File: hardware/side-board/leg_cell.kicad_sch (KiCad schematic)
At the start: 88 parts, among them IC201 STM32C092KCT6, IC202 TCAN332DR, IC203 TPS56A37RPAR, IC204 INA181A1IDBVR, J201 Servo Connector, J202 Servo Connector, J203 Servo Connector, J205 Conn_01x04, Y201 Crystal_GND24

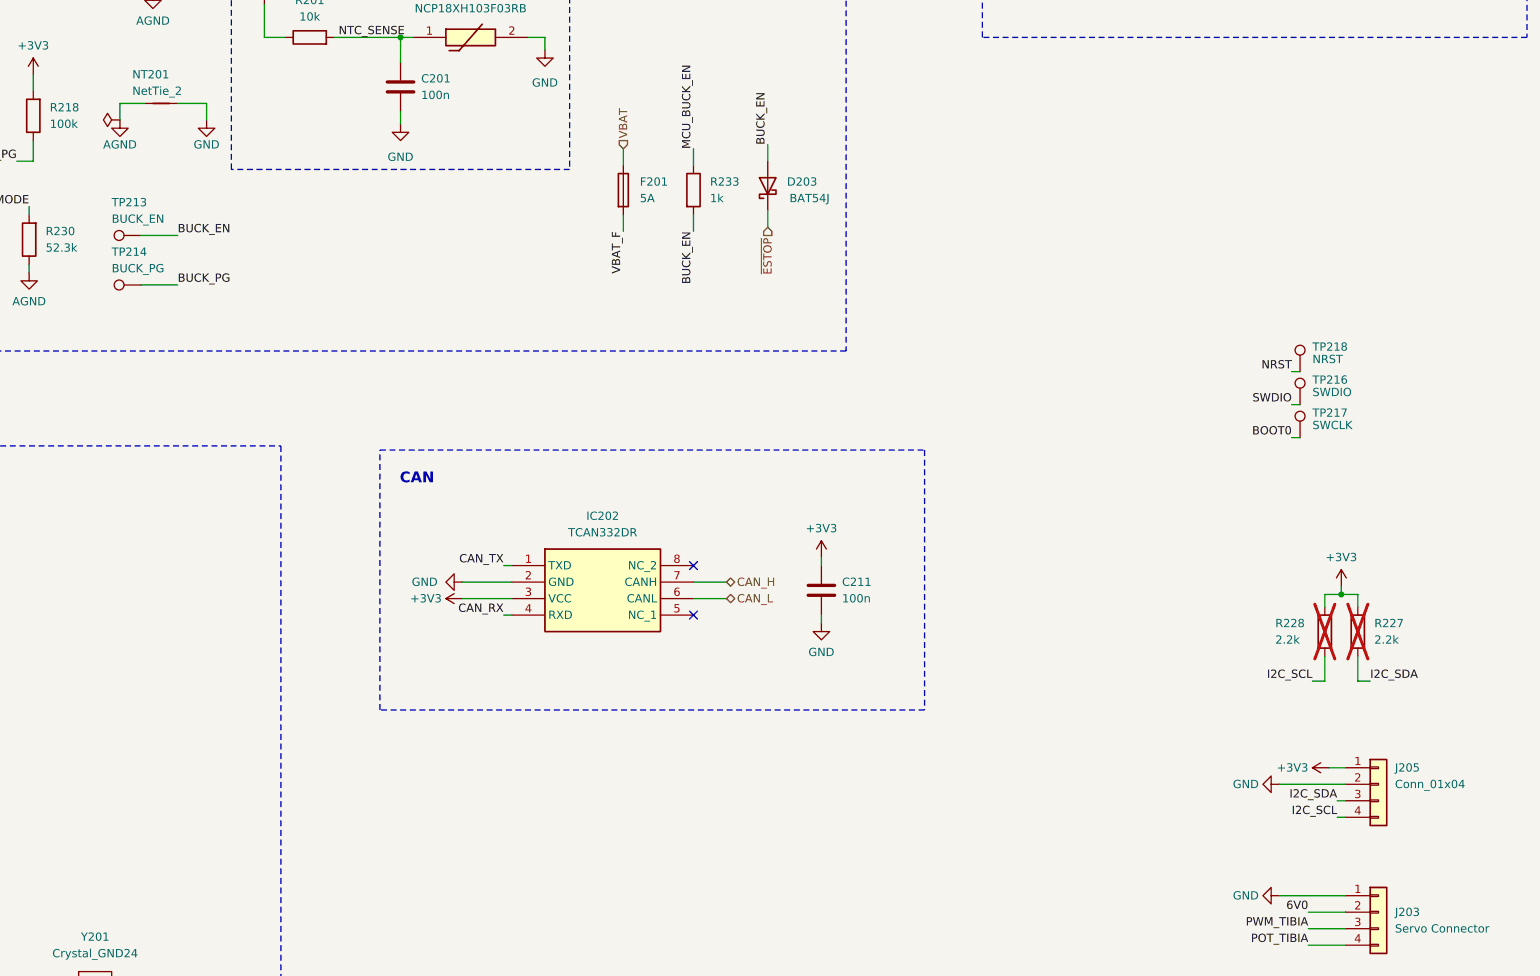
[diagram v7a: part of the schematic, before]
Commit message: Compacted sideboard further
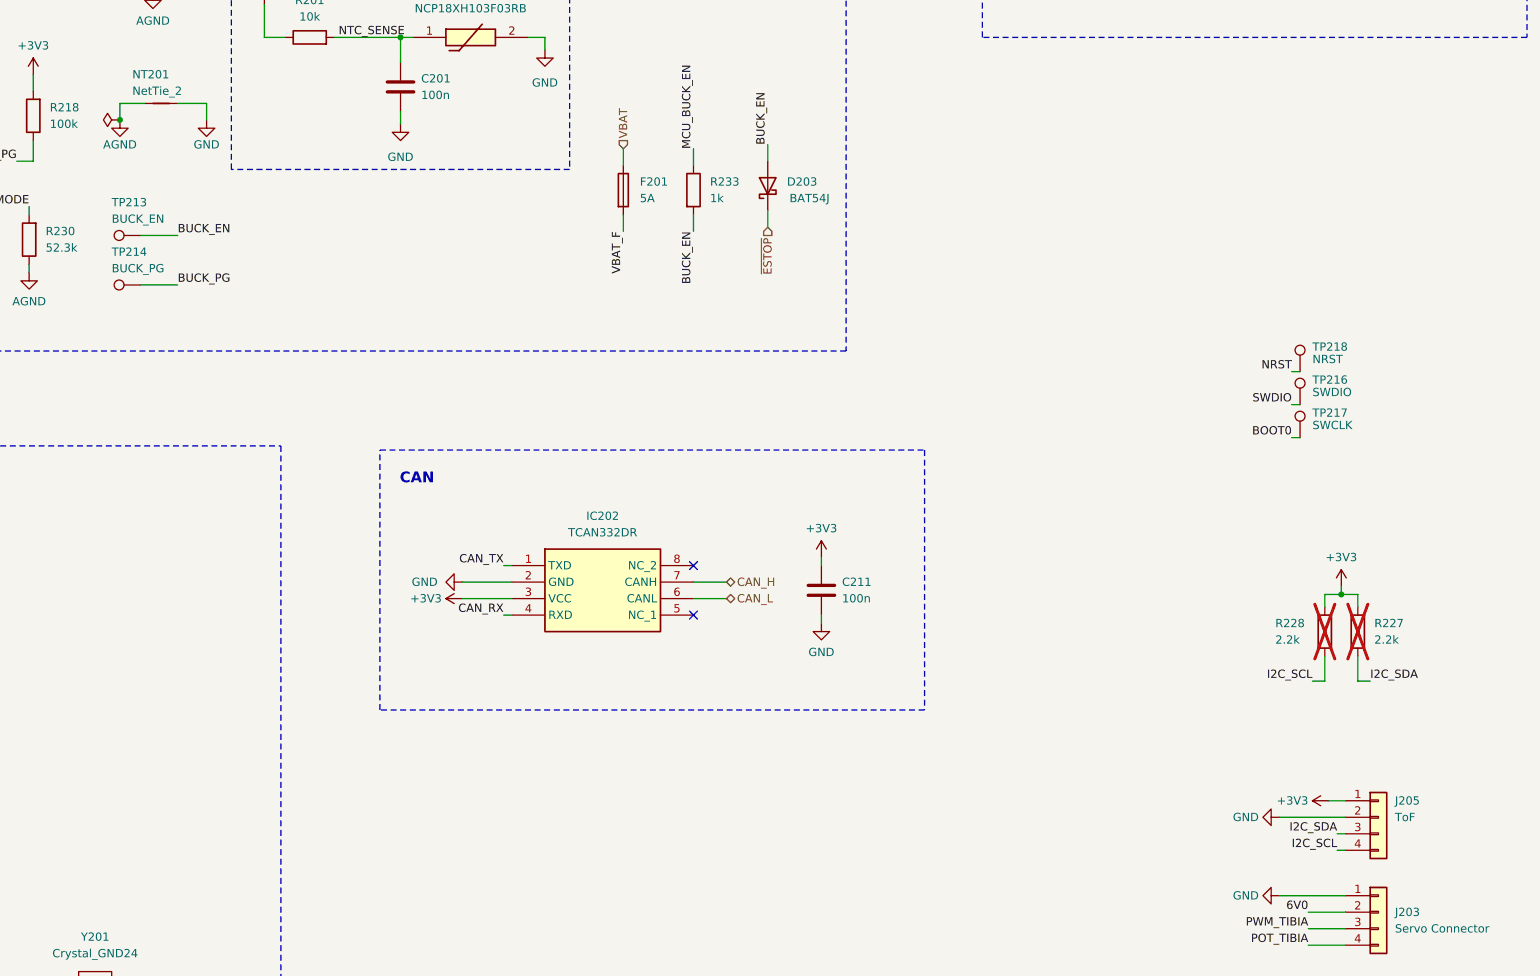
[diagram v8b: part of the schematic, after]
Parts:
- J201, J202, J203: footprint Connector_JST:JST_XH_B4B-XH-A_1x04_P2.50mm_Vertical -> vector:PinHeader_1x04_P2.54mm_Vertical_Tile
- J205: value Conn_01x04 -> ToF; footprint Connector_JST:JST_XH_B4B-XH-A_1x04_P2.50mm_Vertical -> vector:PinHeader_1x04_P2.54mm_Vertical_Tile
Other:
- moved on the sheet: J205
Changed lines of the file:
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@@
 	)
 	(junction
+		(at 184.15 86.36)
+		(diameter 0)
+		(color 0 0 0 0)
+	)
+	(junction
 		(at 260.35 43.18)
 		(diameter 0)
@@
 	)
 	(no_connect
-		(at 76.2 39.37)
+		(at 272.415 162.56)
 	)
 	(no_connect
@@
 	)
 	(no_connect
-		(at 272.415 162.56)
+		(at 272.415 154.94)
 	)
 	(no_connect
-		(at 272.415 154.94)
+		(at 76.2 39.37)
 	)
 	(wire
@@
 	(wire
 		(pts
-			(xy 362.585 188.595) (xy 372.745 188.595)
+			(xy 362.585 193.675) (xy 372.745 193.675)
 		)
 		(stroke
@@
 	(wire
 		(pts
-			(xy 371.475 193.675) (xy 372.745 193.675)
+			(xy 371.475 198.755) (xy 372.745 198.755)
 		)
 		(stroke
@@
 	(wire
 		(pts
-			(xy 370.205 186.055) (xy 372.745 186.055)
+			(xy 370.205 191.135) (xy 372.745 191.135)
 		)
 		(stroke
@@
 	(wire
 		(pts
-			(xy 371.475 191.135) (xy 372.745 191.135)
+			(xy 371.475 196.215) (xy 372.745 196.215)
 		)
 		(stroke
@@
 	)
 	(label "I2C_SCL"
-		(at 371.475 193.675 180)
+		(at 371.475 198.755 180)
 		(effects
 			(font
@@
 	)
 	(label "I2C_SDA"
-		(at 371.475 191.135 180)
+		(at 371.475 196.215 180)
 		(effects
 			(font
@@
 	(symbol
 		(lib_id "Connector_Generic:Conn_01x04")
-		(at 377.825 188.595 0)
+		(at 377.825 193.675 0)
 		(unit 1)
 		(body_style 1)
@@
 		(fields_autoplaced yes)
 		(property "Reference" "J205"
-			(at 380.365 186.0549 0)
+			(at 380.365 191.1349 0)
 			(show_name no)
 			(do_not_autoplace no)
@@
 			)
 		)
-		(property "Value" "Conn_01x04"
-			(at 380.365 188.5949 0)
+		(property "Value" "ToF"
+			(at 380.365 193.6749 0)
 			(show_name no)
 			(do_not_autoplace no)
@@
 			)
 		)
-		(property "Footprint" "Connector_JST:JST_XH_B4B-XH-A_1x04_P2.50mm_Vertical"
-			(at 377.825 188.595 0)
+		(property "Footprint" "vector:PinHeader_1x04_P2.54mm_Vertical_Tile"
+			(at 377.825 193.675 0)
 			(hide yes)
 			(show_name no)
@@
 		)
 		(property "Datasheet" ""
-			(at 377.825 188.595 0)
+			(at 377.825 193.675 0)
 			(hide yes)
 			(show_name no)
@@
 		)
 		(property "Description" "Generic connector, single row, 01x04, script generated (kicad-library-utils/schlib/autogen/connector/)"
-			(at 377.825 188.595 0)
+			(at 377.825 193.675 0)
 			(hide yes)
 			(show_name no)
@@
 	(symbol
 		(lib_id "power:GND")
-		(at 362.585 188.595 270)
+		(at 362.585 193.675 270)
 		(unit 1)
 		(body_style 1)
@@
 		(fields_autoplaced yes)
 		(property "Reference" "#PWR0224"
-			(at 356.235 188.595 0)
+			(at 356.235 193.675 0)
 			(hide yes)
 			(show_name no)
@@
 		)
 		(property "Value" "GND"
-			(at 359.41 188.5949 90)
+			(at 359.41 193.6749 90)
 			(show_name no)
 			(do_not_autoplace no)
@@
 		)
 		(property "Footprint" ""
-			(at 362.585 188.595 0)
+			(at 362.585 193.675 0)
 			(hide yes)
 			(show_name no)
@@
 		)
 		(property "Datasheet" ""
-			(at 362.585 188.595 0)
+			(at 362.585 193.675 0)
 			(hide yes)
 			(show_name no)
@@
 		)
 		(property "Description" "Power symbol creates a global label with name \"GND\" , ground"
-			(at 362.585 188.595 0)
+			(at 362.585 193.675 0)
 			(hide yes)
 			(show_name no)
@@
 			)
 		)
-		(property "Footprint" "Connector_JST:JST_XH_B4B-XH-A_1x04_P2.50mm_Vertical"
+		(property "Footprint" "vector:PinHeader_1x04_P2.54mm_Vertical_Tile"
 			(at 377.825 208.28 0)
 			(hide yes)
@@
 			)
 		)
-		(property "Footprint" "Connector_JST:JST_XH_B4B-XH-A_1x04_P2.50mm_Vertical"
+		(property "Footprint" "vector:PinHeader_1x04_P2.54mm_Vertical_Tile"
 			(at 377.825 237.49 0)
 			(hide yes)
@@
 	(symbol
 		(lib_id "power:+3V3")
-		(at 370.205 186.055 90)
+		(at 370.205 191.135 90)
 		(unit 1)
 		(body_style 1)
@@
 		(fields_autoplaced yes)
 		(property "Reference" "#PWR0225"
-			(at 374.015 186.055 0)
+			(at 374.015 191.135 0)
 			(hide yes)
 			(show_name no)
@@
 		)
 		(property "Value" "+3V3"
-			(at 367.03 186.0549 90)
+			(at 367.03 191.1349 90)
 			(show_name no)
 			(do_not_autoplace no)
@@
 		)
 		(property "Footprint" ""
-			(at 370.205 186.055 0)
+			(at 370.205 191.135 0)
 			(hide yes)
 			(show_name no)
@@
 		)
 		(property "Datasheet" ""
-			(at 370.205 186.055 0)
+			(at 370.205 191.135 0)
 			(hide yes)
 			(show_name no)
@@
 		)
 		(property "Description" "Power symbol creates a global label with name \"+3V3\""
-			(at 370.205 186.055 0)
+			(at 370.205 191.135 0)
 			(hide yes)
 			(show_name no)
@@
 			)
 		)
-		(property "Footprint" "Connector_JST:JST_XH_B4B-XH-A_1x04_P2.50mm_Vertical"
+		(property "Footprint" "vector:PinHeader_1x04_P2.54mm_Vertical_Tile"
 			(at 377.825 222.885 0)
 			(hide yes)
